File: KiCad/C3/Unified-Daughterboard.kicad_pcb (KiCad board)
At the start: 2 copper layers, 18 x 16.5 mm, 14 parts, among them J1 TYPE-C-31-M12_13, J2 SM04B-SRSS-TB(LF)(SN), U1 TPD4E05U06DQAR

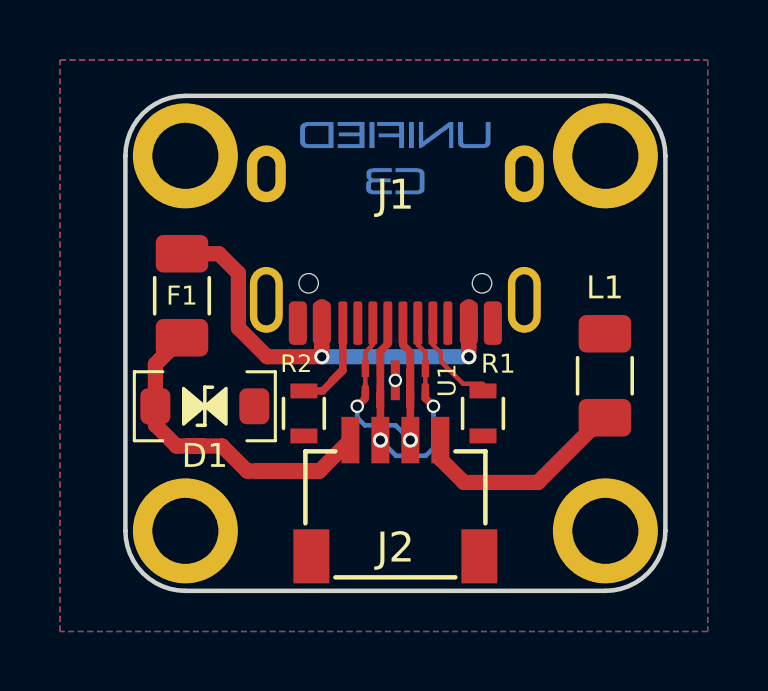
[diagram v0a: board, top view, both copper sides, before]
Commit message: various optimizations to schematic and layout
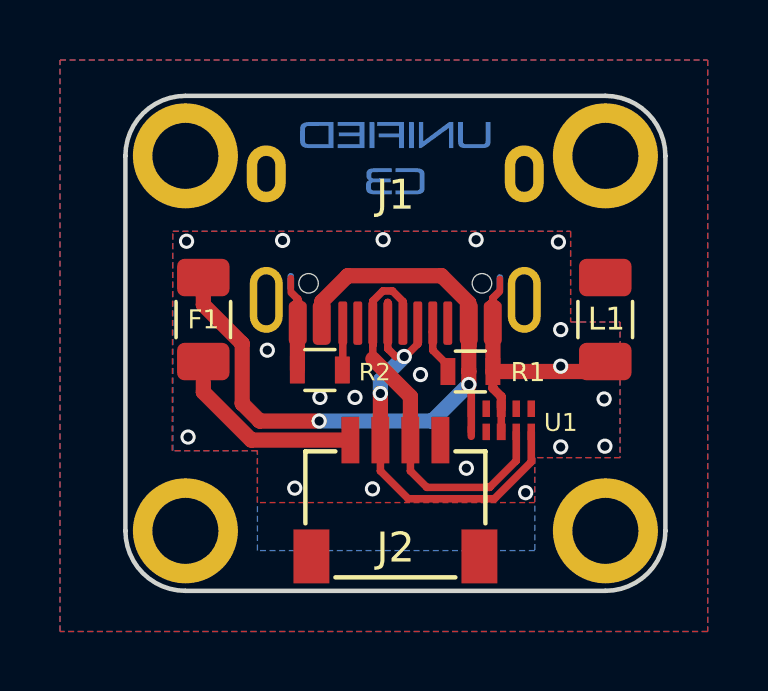
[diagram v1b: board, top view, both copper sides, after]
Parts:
- removed D1: SMF9.0CA, acheron_Components:D_SOD-123_Bidirectional
- MH1, MH2, MH3, MH4: footprint random-keyboard-parts:Generic-Mounthole -> MountingHole:MountingHole_2.2mm_M2_ISO7380_Pad
- moved U1 3.77 mm to (78.5, 67.4)
- moved L1 1.87 mm to (82.0, 64.0), turned to 270 degrees
- moved R2 1.54 mm to (72.5, 65.7), turned to 180 degrees
- moved R1 1.46 mm to (77.5, 65.7), turned to 0 degrees
- moved F1 1.07 mm to (68.6, 64.0)
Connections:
- J1 pad A1: GNDPWR -> GND
- J1 pad A6: DA+ -> DP
- J1 pad A7: DA- -> DN
- J1 pad B1: GNDPWR -> GND
- J1 pad B6: DA+ -> DP
- J1 pad B7: DA- -> DN
- J2 pad : (no net) -> GNDPWR
- J2 pad 2: DA- -> DN
- J2 pad 3: DA+ -> DP
- L1 pad 1: GND -> GNDPWR
- L1 pad 2: GNDPWR -> GND
- R1 pad 2: GNDPWR -> GND
- R2 pad 2: GNDPWR -> GND
- U1 pad 1: DA+ -> VBUS
- U1 pad 10: DA+ -> VBUS
- U1 pad 2: DA- -> Net-(U1-Pad2)
- U1 pad 3: GNDPWR -> GND
- U1 pad 4: DA+ -> DP
- U1 pad 5: DA- -> DN
- U1 pad 6: DA- -> Net-(U1-Pad6)
- U1 pad 7: DA+ -> Net-(U1-Pad7)
- U1 pad 8: GNDPWR -> GND
- U1 pad 9: DA- -> Net-(U1-Pad9)
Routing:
- net DN: track 0.00 -> 15.1 mm, vias 0 -> 2
- net DP: track 0.00 -> 14.5 mm
- net DA+: track 13.6 -> 0.00 mm, vias 2 -> 0
- net DA-: track 13.4 -> 0.00 mm, vias 2 -> 0
- net VBUS: track 15.4 -> 25.3 mm
- net VCC: track 14.7 -> 6.12 mm
- net GND: track 7.36 -> 12.4 mm, vias 0 -> 19
- net Net-(J1-PadB5): track 6.33 -> 4.16 mm
- net Net-(J1-PadA5): track 3.84 -> 2.56 mm
- net GNDPWR: track 0.14 -> 0.23 mm, vias 1 -> 0
- added copper zone on B.Cu, net GND
- added copper zone on F.Cu, net GND
